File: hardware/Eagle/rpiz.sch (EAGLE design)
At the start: 19 parts, among them Q1 2N5484, Q2 2N5484

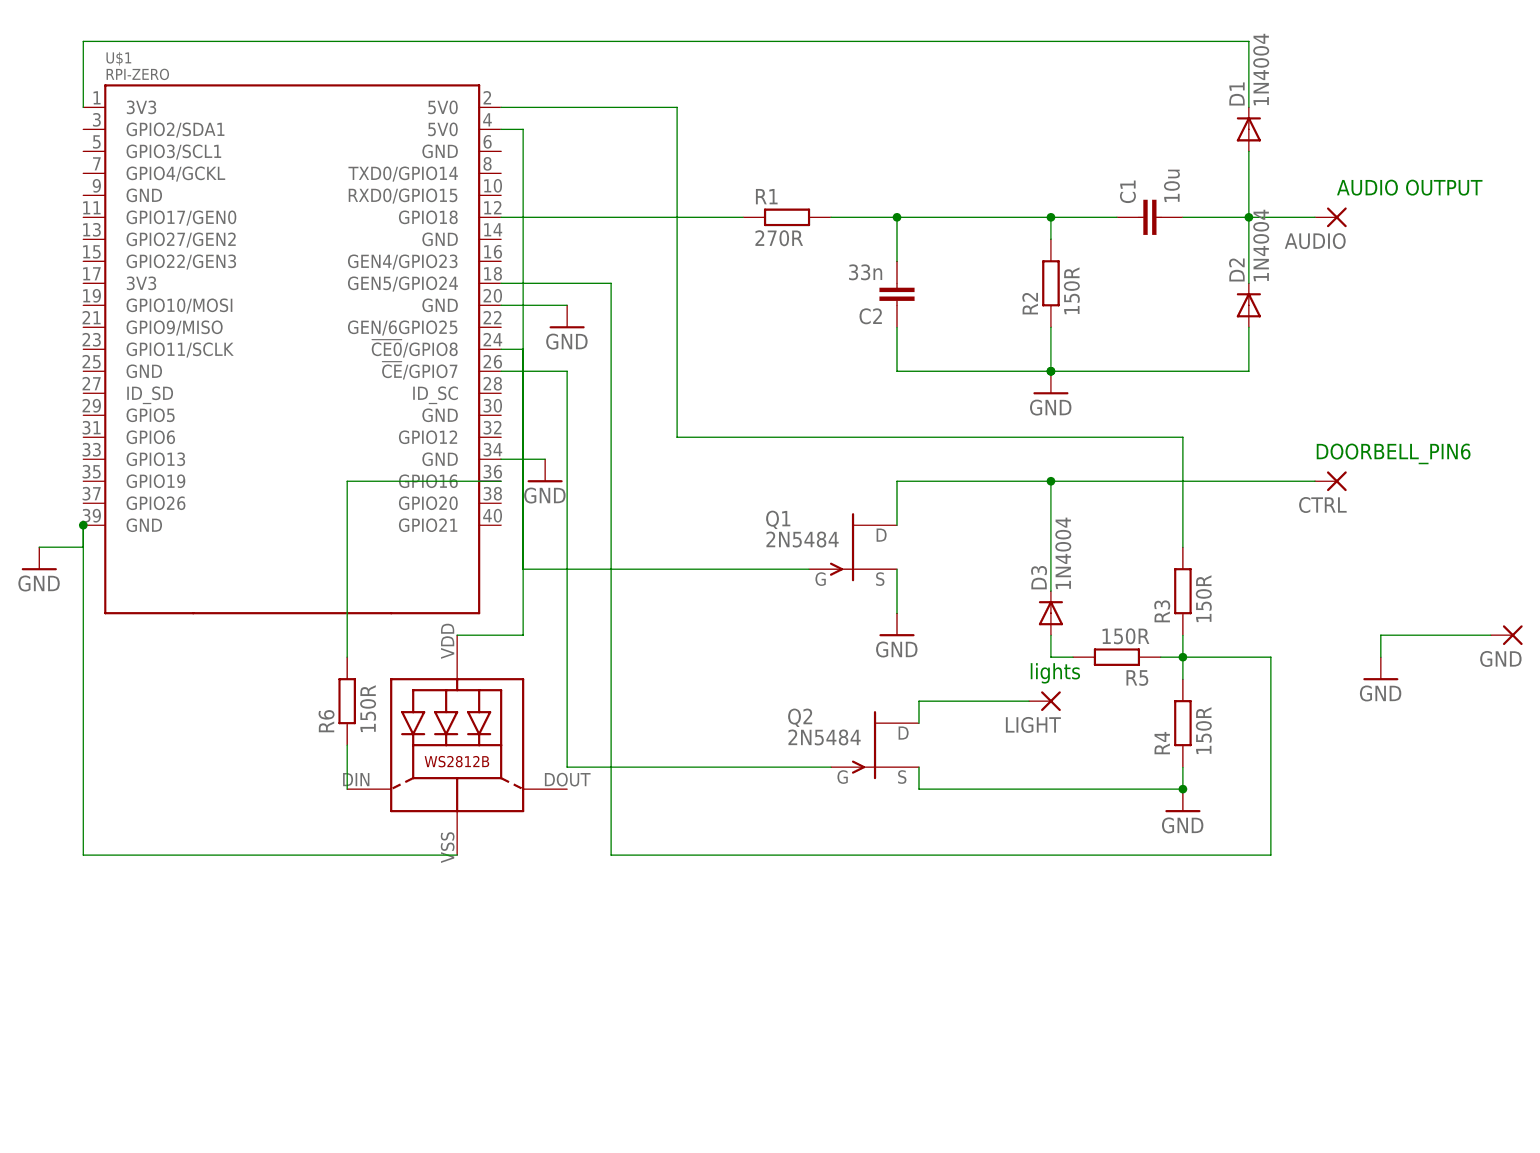
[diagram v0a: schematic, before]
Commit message: board is now using 2n7000 mosfet, also added 2nd LED
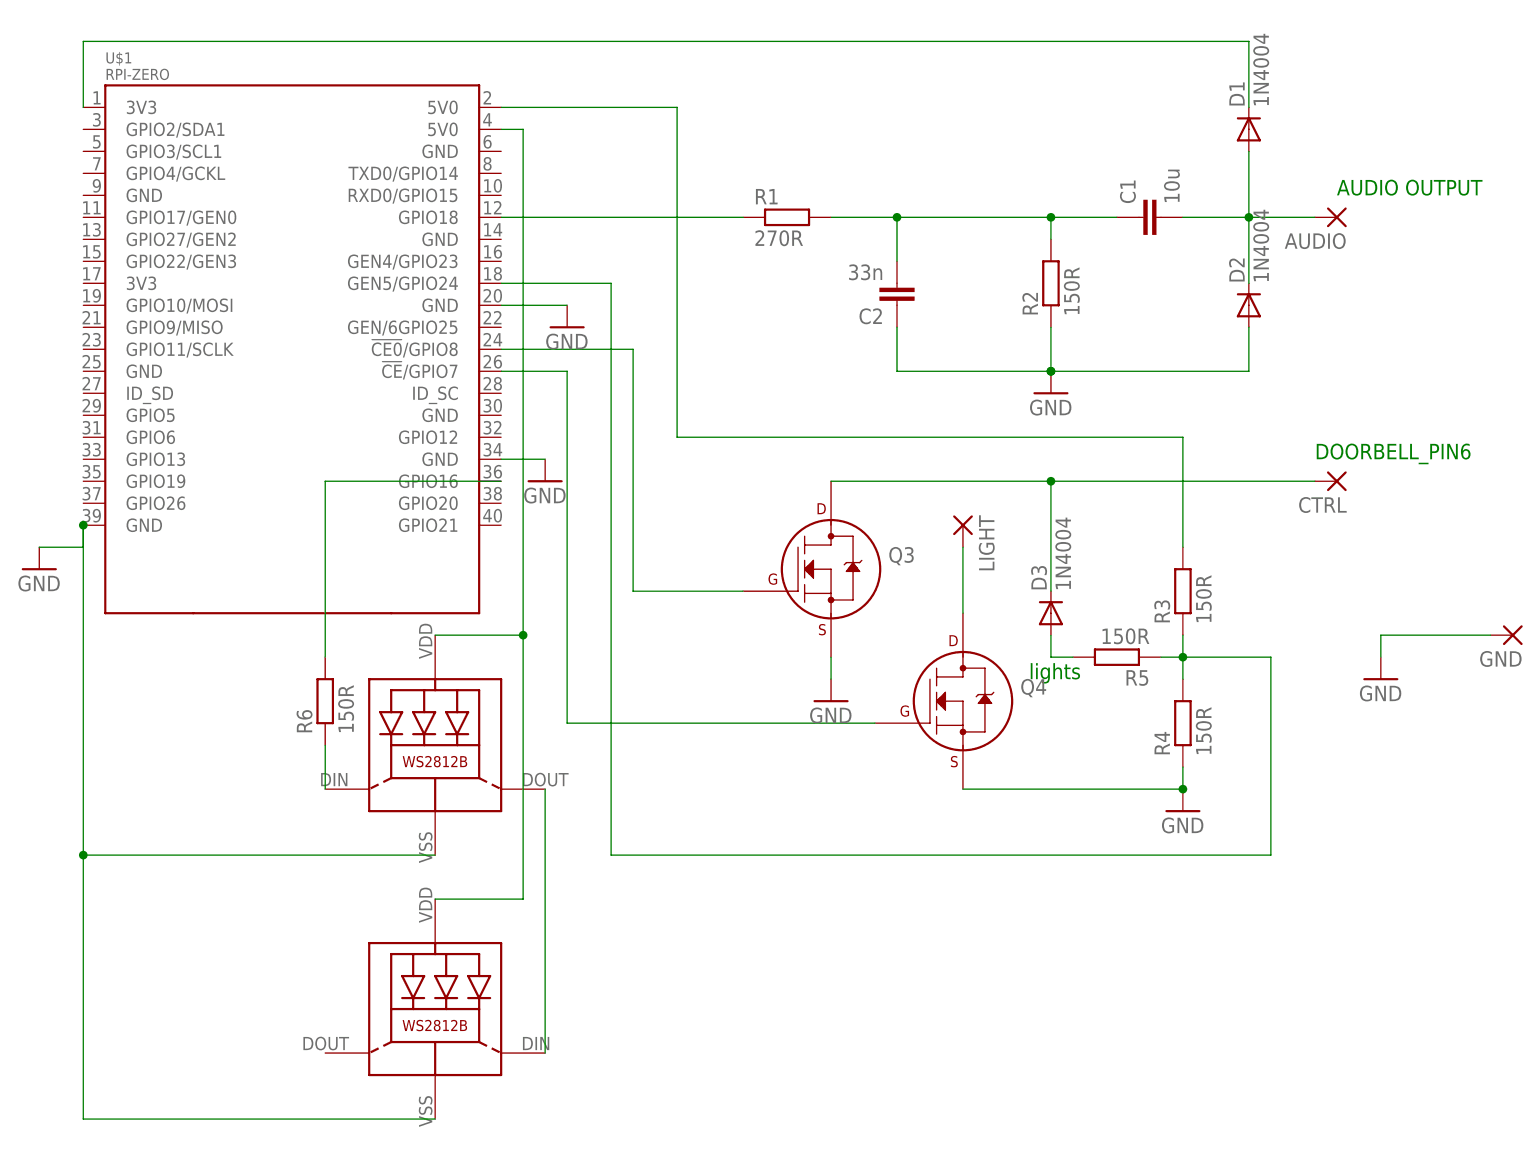
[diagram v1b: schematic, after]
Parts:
- removed Q1, Q2: 2N5484, transistor-fet:2N5484
- added LED2: WS2812B, WS2812B:WS2812B
- added Q3, Q4: (no value), transistors:2N7000_TO92
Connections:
- new net N$11: LED1.DO, LED2.DI
- net 5V0@2: now also LED2.VDD
- net GND: now also LED2.GND, Q3.S, Q4.S; no longer Q1.S, Q2.S
- net N$2: now also Q3.D; no longer Q1.D
- net N$3: now also Q3.G; no longer Q1.G
- net N$7: now also Q4.G; no longer Q2.G
- net N$9: now also Q4.D; no longer Q2.D
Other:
- moved on the sheet: LIGHT, R6
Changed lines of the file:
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@@
 <part name="D1" library="diode" deviceset="1N4004" device=""/>
 <part name="D2" library="diode" deviceset="1N4004" device=""/>
-<part name="Q1" library="transistor-fet" deviceset="?548*" device="2N" technology="4"/>
 <part name="GND2" library="supply1" deviceset="GND" device=""/>
 <part name="D3" library="diode" deviceset="1N4004" device=""/>
@@
 <part name="GND4" library="supply1" deviceset="GND" device=""/>
 <part name="GND5" library="supply1" deviceset="GND" device=""/>
-<part name="Q2" library="transistor-fet" deviceset="?548*" device="2N" technology="4"/>
 <part name="LIGHT" library="wirepad" deviceset="2,15/1,0" device=""/>
 <part name="CTRL" library="wirepad" deviceset="2,15/1,0" device=""/>
@@
 <attribute name="SPICEPREFIX" value="150R"/>
 </part>
+<part name="Q3" library="transistors" deviceset="2N700*" device="_TO92" technology="0"/>
+<part name="Q4" library="transistors" deviceset="2N700*" device="_TO92" technology="0"/>
+<part name="LED2" library="WS2812B" deviceset="WS2812B" device=""/>
 </parts>
 <sheets>
@@
 <instance part="D1" gate="1" x="134.62" y="73.66" rot="R90"/>
 <instance part="D2" gate="1" x="134.62" y="53.34" rot="R90"/>
-<instance part="Q1" gate="G$1" x="88.9" y="25.4"/>
-<instance part="GND2" gate="1" x="93.98" y="15.24"/>
+<instance part="GND2" gate="1" x="86.36" y="7.62"/>
 <instance part="D3" gate="1" x="111.76" y="17.78" rot="R90"/>
 <instance part="R3" gate="G$1" x="127" y="20.32" rot="R90"/>
@@
 <instance part="GND4" gate="1" x="55.88" y="50.8"/>
 <instance part="GND5" gate="1" x="127" y="-5.08"/>
-<instance part="Q2" gate="G$1" x="91.44" y="2.54"/>
-<instance part="LIGHT" gate="1" x="111.76" y="7.62" rot="R180"/>
+<instance part="LIGHT" gate="1" x="101.6" y="27.94" rot="R270"/>
 <instance part="CTRL" gate="1" x="144.78" y="33.02" rot="R180"/>
 <instance part="AUDIO" gate="1" x="144.78" y="63.5" rot="R180"/>
 <instance part="GND6" gate="1" x="149.86" y="10.16"/>
 <instance part="GND" gate="1" x="165.1" y="15.24" rot="R180"/>
-<instance part="LED1" gate="G$1" x="43.18" y="0"/>
+<instance part="LED1" gate="G$1" x="40.64" y="0"/>
 <instance part="GND7" gate="1" x="53.34" y="33.02"/>
-<instance part="R6" gate="G$1" x="30.48" y="7.62" rot="R90"/>
+<instance part="R6" gate="G$1" x="27.94" y="7.62" rot="R90"/>
+<instance part="Q3" gate="G$1" x="86.36" y="22.86"/>
+<instance part="Q4" gate="G$1" x="101.6" y="7.62"/>
+<instance part="LED2" gate="G$1" x="40.64" y="-30.48" rot="MR0"/>
 </instances>
 <busses>
@@
 </segment>
 <segment>
-<pinref part="Q1" gate="G$1" pin="S"/>
-<pinref part="GND2" gate="1" pin="GND"/>
-<wire x1="93.98" y1="22.86" x2="93.98" y2="17.78" width="0.1524" layer="91"/>
-</segment>
-<segment>
 <pinref part="GND3" gate="1" pin="GND"/>
 <pinref part="U$1" gate="G$1" pin="GND@3"/>
@@
 <wire x1="0" y1="25.4" x2="0" y2="27.94" width="0.1524" layer="91"/>
 <pinref part="LED1" gate="G$1" pin="GND"/>
-<wire x1="43.18" y1="-10.16" x2="0" y2="-10.16" width="0.1524" layer="91"/>
+<wire x1="40.64" y1="-10.16" x2="0" y2="-10.16" width="0.1524" layer="91"/>
 <wire x1="0" y1="-10.16" x2="0" y2="27.94" width="0.1524" layer="91"/>
 <junction x="0" y="27.94"/>
+<pinref part="LED2" gate="G$1" pin="GND"/>
+<wire x1="40.64" y1="-40.64" x2="0" y2="-40.64" width="0.1524" layer="91"/>
+<wire x1="0" y1="-40.64" x2="0" y2="-10.16" width="0.1524" layer="91"/>
+<junction x="0" y="-10.16"/>
 </segment>
 <segment>
@@
 <pinref part="R4" gate="G$1" pin="1"/>
 <wire x1="127" y1="-2.54" x2="127" y2="0" width="0.1524" layer="91"/>
-<pinref part="Q2" gate="G$1" pin="S"/>
-<wire x1="96.52" y1="0" x2="96.52" y2="-2.54" width="0.1524" layer="91"/>
-<wire x1="96.52" y1="-2.54" x2="127" y2="-2.54" width="0.1524" layer="91"/>
+<wire x1="101.6" y1="-2.54" x2="127" y2="-2.54" width="0.1524" layer="91"/>
 <junction x="127" y="-2.54"/>
+<pinref part="Q4" gate="G$1" pin="S"/>
 </segment>
 <segment>
@@
 <pinref part="U$1" gate="G$1" pin="GND@7"/>
 <wire x1="53.34" y1="35.56" x2="48.26" y2="35.56" width="0.1524" layer="91"/>
+</segment>
+<segment>
+<pinref part="Q3" gate="G$1" pin="S"/>
+<pinref part="GND2" gate="1" pin="GND"/>
+<wire x1="86.36" y1="10.16" x2="86.36" y2="12.7" width="0.1524" layer="91"/>
 </segment>
 </net>
@@
 <net name="N$2" class="0">
 <segment>
-<pinref part="Q1" gate="G$1" pin="D"/>
-<wire x1="93.98" y1="27.94" x2="93.98" y2="33.02" width="0.1524" layer="91"/>
-<wire x1="93.98" y1="33.02" x2="111.76" y2="33.02" width="0.1524" layer="91"/>
+<wire x1="86.36" y1="33.02" x2="111.76" y2="33.02" width="0.1524" layer="91"/>
 <pinref part="D3" gate="1" pin="C"/>
 <wire x1="111.76" y1="33.02" x2="142.24" y2="33.02" width="0.1524" layer="91"/>
@@
 <junction x="111.76" y="33.02"/>
 <pinref part="CTRL" gate="1" pin="P"/>
+<pinref part="Q3" gate="G$1" pin="D"/>
 </segment>
 </net>
@@
 <net name="N$7" class="0">
 <segment>
-<pinref part="Q2" gate="G$1" pin="G"/>
-<wire x1="86.36" y1="0" x2="55.88" y2="0" width="0.1524" layer="91"/>
-<wire x1="55.88" y1="0" x2="55.88" y2="45.72" width="0.1524" layer="91"/>
+<wire x1="91.44" y1="5.08" x2="55.88" y2="5.08" width="0.1524" layer="91"/>
+<wire x1="55.88" y1="5.08" x2="55.88" y2="45.72" width="0.1524" layer="91"/>
 <pinref part="U$1" gate="G$1" pin="!CE!/GPIO7"/>
 <wire x1="55.88" y1="45.72" x2="48.26" y2="45.72" width="0.1524" layer="91"/>
+<pinref part="Q4" gate="G$1" pin="G"/>
 </segment>
 </net>
 <net name="N$9" class="0">
 <segment>
-<pinref part="Q2" gate="G$1" pin="D"/>
-<wire x1="96.52" y1="5.08" x2="96.52" y2="7.62" width="0.1524" layer="91"/>
-<wire x1="96.52" y1="7.62" x2="109.22" y2="7.62" width="0.1524" layer="91"/>
+<wire x1="101.6" y1="17.78" x2="101.6" y2="25.4" width="0.1524" layer="91"/>
 <pinref part="LIGHT" gate="1" pin="P"/>
+<pinref part="Q4" gate="G$1" pin="D"/>
 </segment>
 </net>
 <net name="N$3" class="0">
 <segment>
-<pinref part="Q1" gate="G$1" pin="G"/>
-<wire x1="83.82" y1="22.86" x2="50.8" y2="22.86" width="0.1524" layer="91"/>
-<wire x1="50.8" y1="22.86" x2="50.8" y2="48.26" width="0.1524" layer="91"/>
+<wire x1="63.5" y1="48.26" x2="48.26" y2="48.26" width="0.1524" layer="91"/>
 <pinref part="U$1" gate="G$1" pin="!CE0!/GPIO8"/>
-<wire x1="50.8" y1="48.26" x2="48.26" y2="48.26" width="0.1524" layer="91"/>
+<pinref part="Q3" gate="G$1" pin="G"/>
+<wire x1="76.2" y1="20.32" x2="63.5" y2="20.32" width="0.1524" layer="91"/>
+<wire x1="63.5" y1="20.32" x2="63.5" y2="48.26" width="0.1524" layer="91"/>
 </segment>
 </net>
@@
 <segment>
 <pinref part="LED1" gate="G$1" pin="VDD"/>
-<wire x1="43.18" y1="15.24" x2="50.8" y2="15.24" width="0.1524" layer="91"/>
+<wire x1="40.64" y1="15.24" x2="50.8" y2="15.24" width="0.1524" layer="91"/>
 <wire x1="50.8" y1="15.24" x2="50.8" y2="73.66" width="0.1524" layer="91"/>
 <pinref part="U$1" gate="G$1" pin="5V0@2"/>
 <wire x1="50.8" y1="73.66" x2="48.26" y2="73.66" width="0.1524" layer="91"/>
+<pinref part="LED2" gate="G$1" pin="VDD"/>
+<wire x1="40.64" y1="-15.24" x2="50.8" y2="-15.24" width="0.1524" layer="91"/>
+<wire x1="50.8" y1="-15.24" x2="50.8" y2="15.24" width="0.1524" layer="91"/>
+<junction x="50.8" y="15.24"/>
 </segment>
 </net>
@@
 <pinref part="R6" gate="G$1" pin="1"/>
 <pinref part="LED1" gate="G$1" pin="DI"/>
-<wire x1="30.48" y1="2.54" x2="30.48" y2="-2.54" width="0.1524" layer="91"/>
+<wire x1="27.94" y1="2.54" x2="27.94" y2="-2.54" width="0.1524" layer="91"/>
 </segment>
 </net>
@@
 <pinref part="R6" gate="G$1" pin="2"/>
 <pinref part="U$1" gate="G$1" pin="GPIO16"/>
-<wire x1="30.48" y1="12.7" x2="30.48" y2="33.02" width="0.1524" layer="91"/>
-<wire x1="30.48" y1="33.02" x2="48.26" y2="33.02" width="0.1524" layer="91"/>
-</segment>
-</net>
+<wire x1="27.94" y1="12.7" x2="27.94" y2="33.02" width="0.1524" layer="91"/>
+<wire x1="27.94" y1="33.02" x2="48.26" y2="33.02" width="0.1524" layer="91"/>
+</segment>
+</net>
+<net name="N$11" class="0">
+<segment>
+<pinref part="LED1" gate="G$1" pin="DO"/>
+<pinref part="LED2" gate="G$1" pin="DI"/>
+<wire x1="53.34" y1="-2.54" x2="53.34" y2="-33.02" width="0.1524" layer="91"/>
+</segment>
+</net>
